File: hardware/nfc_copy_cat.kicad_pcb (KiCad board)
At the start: 2 copper layers, 40.4 x 43 mm, 33 parts, among them J1 USB_B_Micro, U1 AP2112K-3.3TRG1, U2 MCP73831-2-OT, U3 TC4424, U4 ATSAMD21E18A

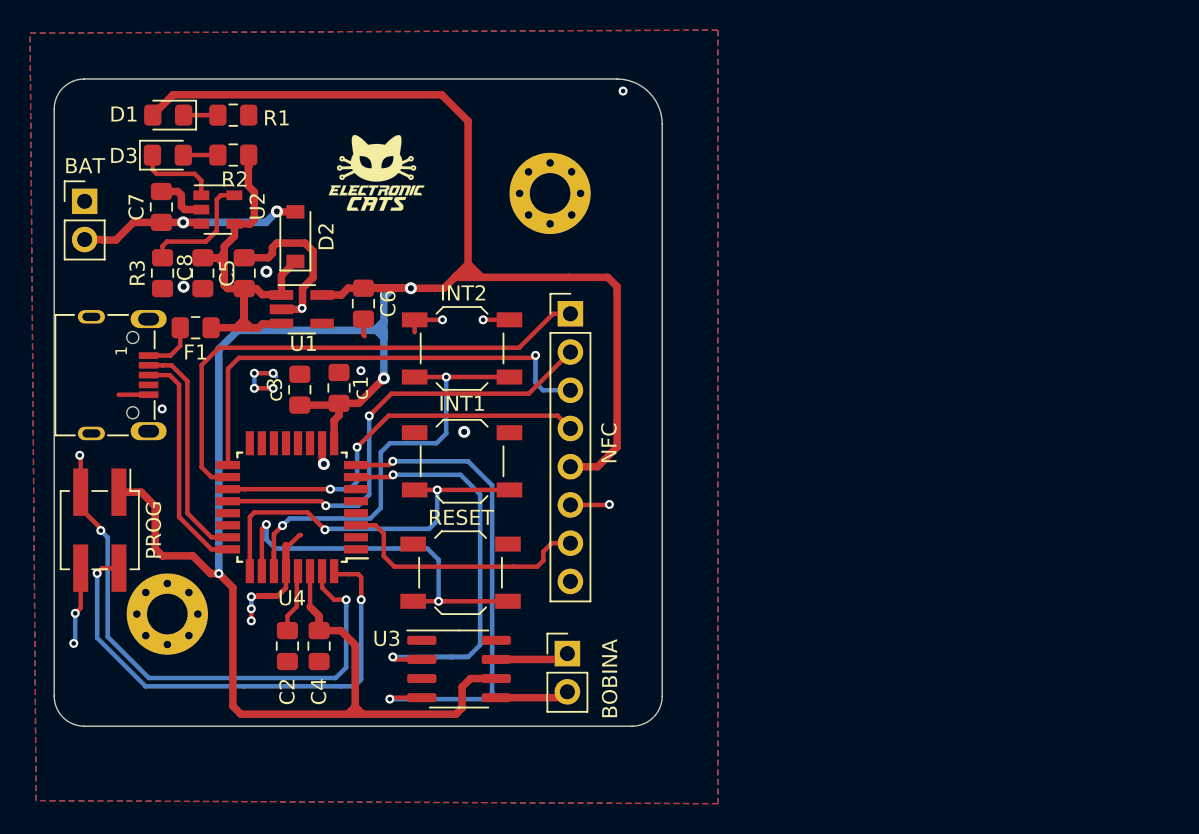
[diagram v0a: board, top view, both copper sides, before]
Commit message: añadimiento de led
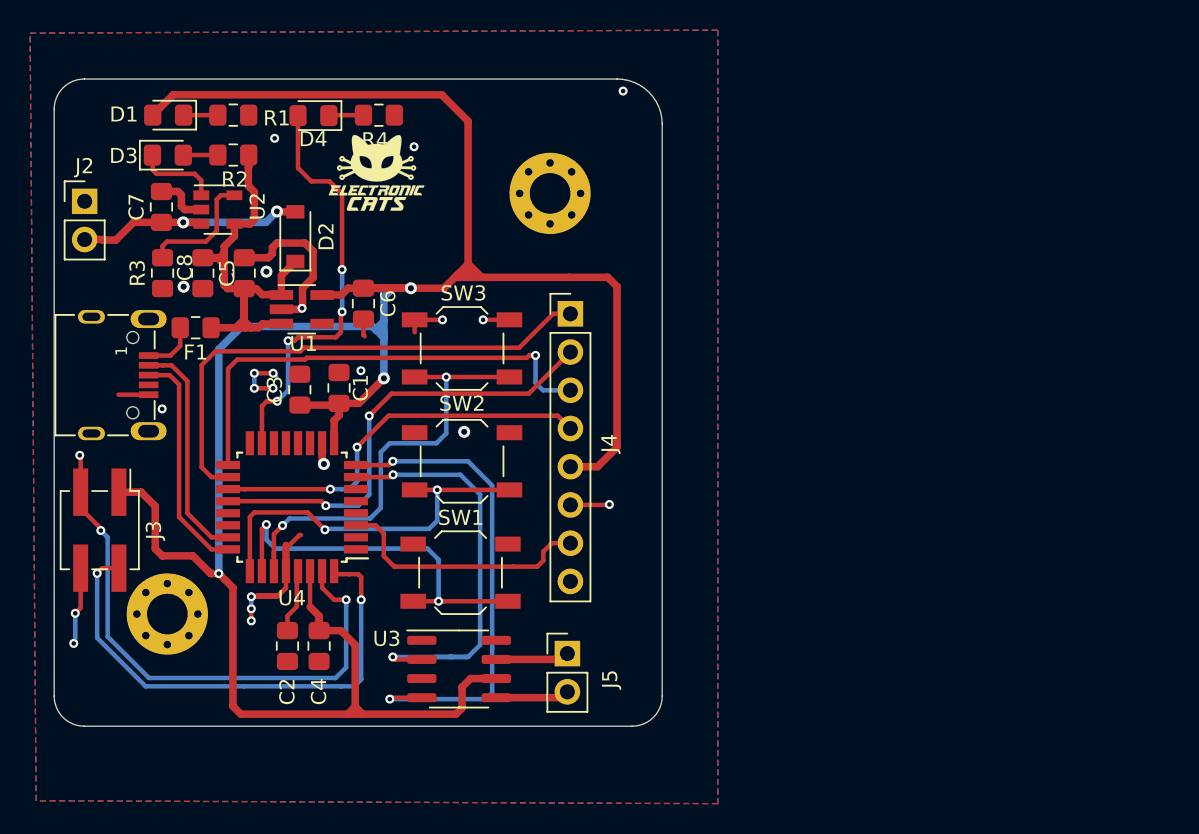
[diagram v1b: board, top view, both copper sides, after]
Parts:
- added D4: LED_Small, LED_SMD:LED_0805_2012Metric_Pad1.15x1.40mm_HandSolder, F.Cu at (144.9, 51.6)
- added R4: 330, Resistor_SMD:R_0805_2012Metric_Pad1.15x1.40mm_HandSolder, F.Cu at (149.3, 51.6)
- C4: value 0.1UF -> 0.1uf
- C6, C7, C8: value C -> 10uf
- R2: value R -> 1k
- R3: value R -> 2.2k
- renumbered c1 to C1, c3 to C3, BAT to J2, PROG to J3, NFC to J4, BOBINA to J5, RESET to SW1, INT1 to SW2, INT2 to SW3
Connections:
- U4 pad 15: Net-(U4-Pad15) -> /2(LED)
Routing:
- net /2(LED): track 0.00 -> 28.0 mm, vias 0 -> 4
- net Net-(D4-Pad1): track 0.00 -> 2.31 mm
- net GND: vias 20 -> 22

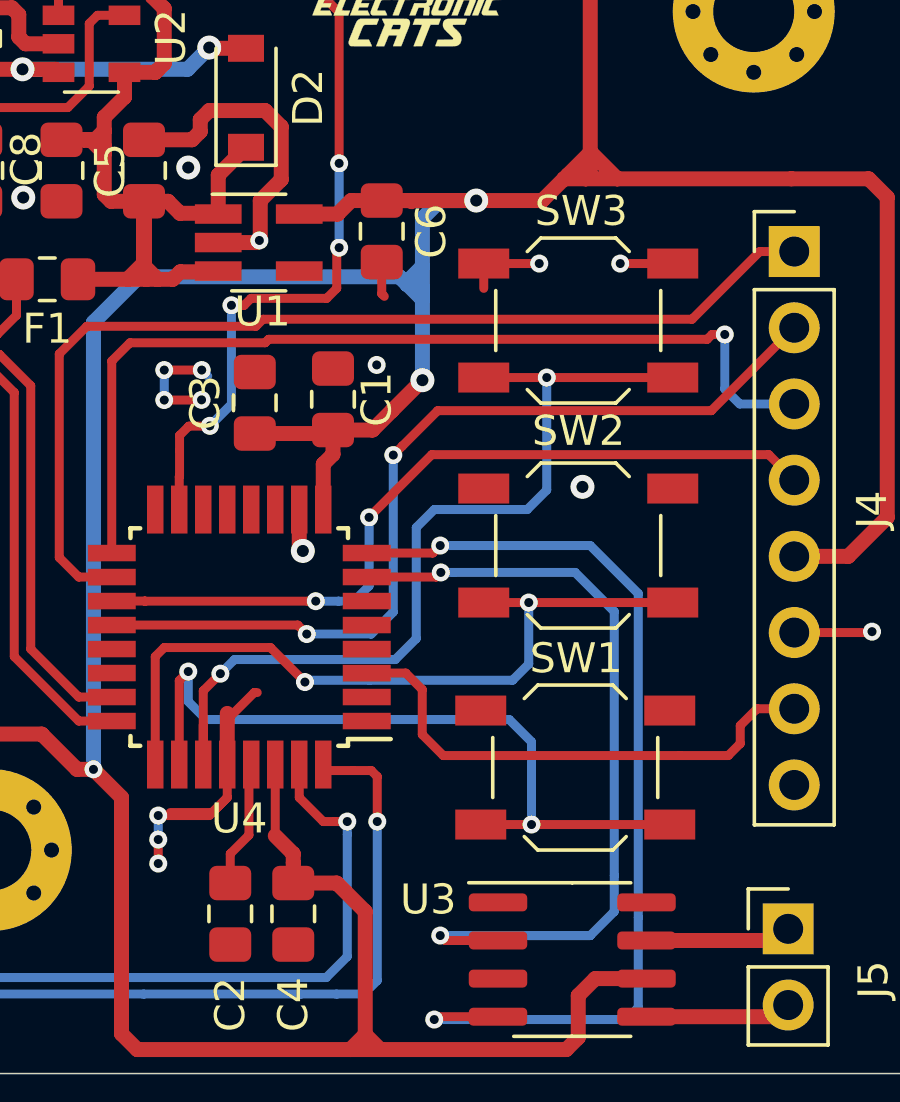
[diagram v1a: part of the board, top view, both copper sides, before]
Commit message: desplazamiento de botones haca atras
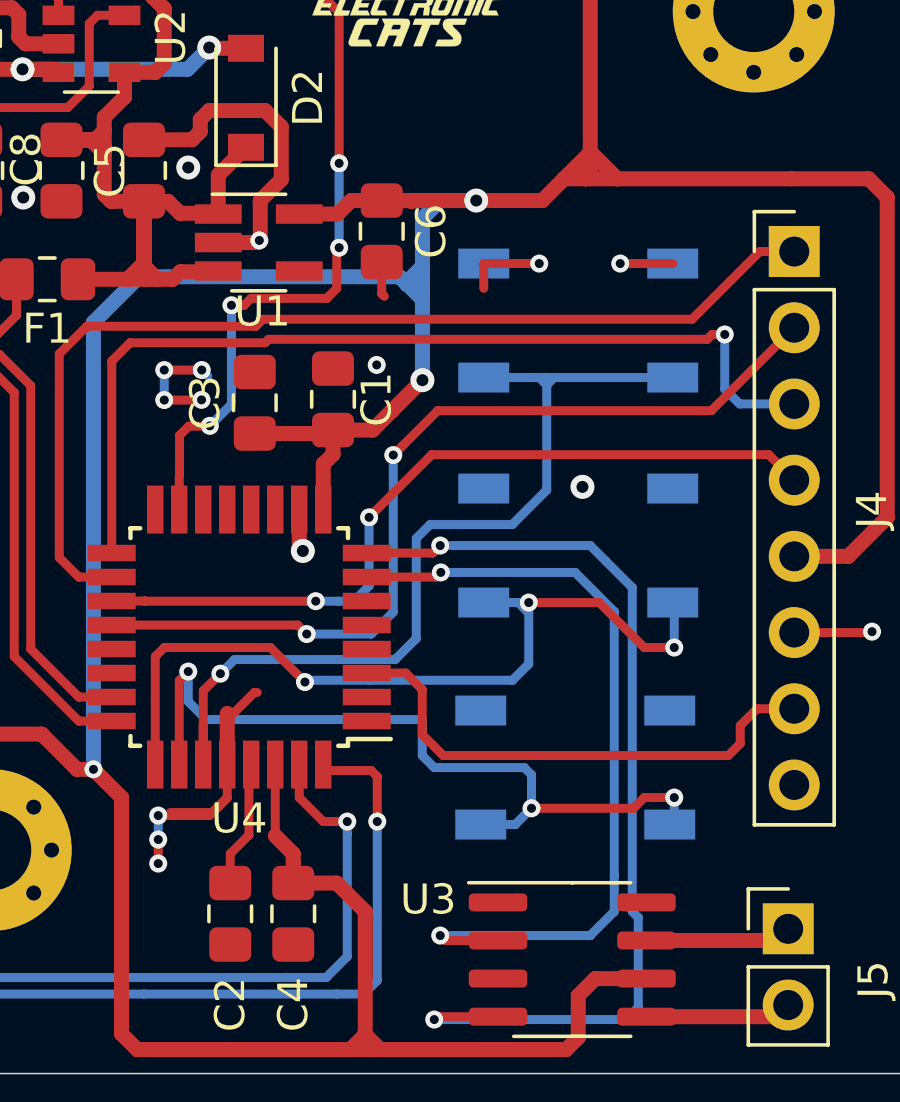
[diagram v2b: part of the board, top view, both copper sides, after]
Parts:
- SW1, SW2, SW3: moved to B.Cu
- turned SW1 to 0 degrees
- turned SW2 to 0 degrees
- turned SW3 to 0 degrees
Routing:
- net /SW1: track 25.2 -> 29.1 mm, vias 2 -> 3
- net /RESET: track 25.3 -> 26.9 mm, vias 2 -> 3
- net /SW2: track 30.2 -> 31.2 mm, vias 2 -> 1

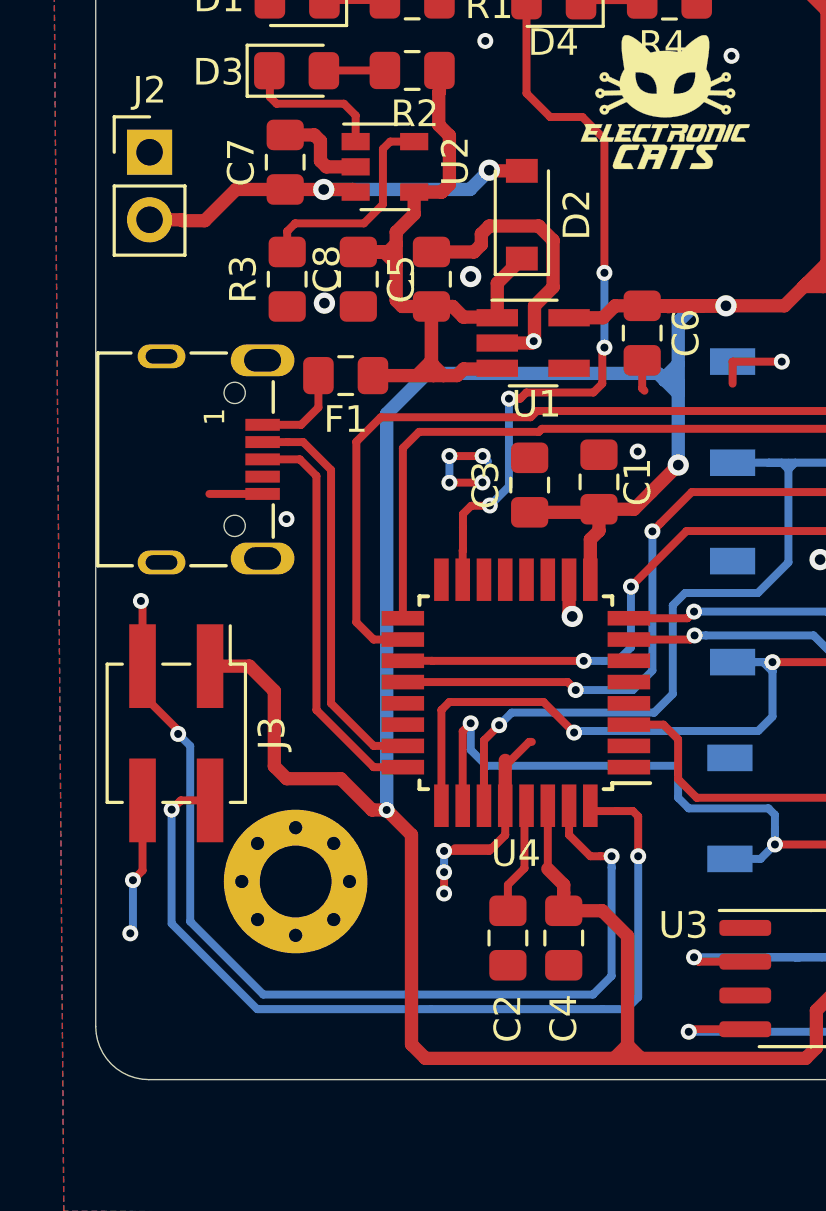
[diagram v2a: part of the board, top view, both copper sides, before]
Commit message: Update traces, USB port and version 1.3v
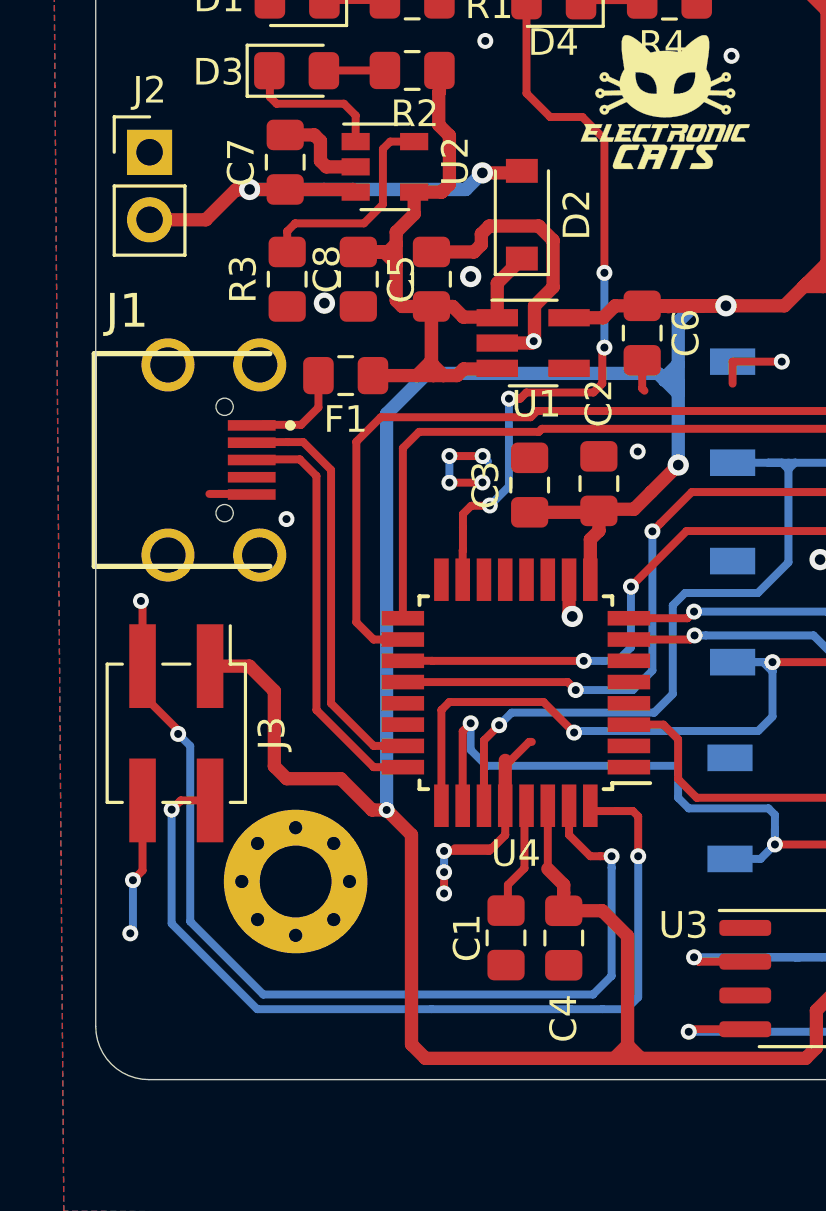
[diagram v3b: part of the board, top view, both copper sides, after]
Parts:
- D1: value LED_Small -> POWER
- D2: value D_Schottky -> MBR120
- D4: value LED_Small -> LED
- J1: footprint Connectors_EC:629105150521 -> Connectors:U254051N4BH806
- J2: value Screw_Terminal_01x02 -> Battery
- J4: value Conn_01x08 -> NFC Module V3
- SW1: value SW_DPST_x2 -> RST
- SW2: value SW_DPST_x2 -> Magspoof
- SW3: value SW_DPST_x2 -> NFC
- moved C1 17.5 mm to (143.1, 86.9), turned to 270 degrees
- moved C2 17.4 mm to (146.6, 69.8), turned to 90 degrees
- moved J1 1.54 mm to (131.4, 68.9)
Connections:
- net /2(LED) renamed /LED1
- net /BAT renamed +BATT
- net Net-(U4-Pad13) renamed /LED3
- net Net-(U4-Pad14) renamed /LED2
- C1 pad 1: +3V3 -> Net-(C1-Pad1)
- C2 pad 1: Net-(C2-Pad1) -> +3V3
- U4 pad 29: Net-(C2-Pad1) -> Net-(C1-Pad1)
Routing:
- net Net-(C2-Pad1): track 4.20 -> 0.00 mm
- net Net-(C1-Pad1): track 0.00 -> 4.20 mm
- net +BATT: track 16.1 -> 18.8 mm
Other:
- board text added: "NFC COPY CAT v1.2"
- board text removed: "NFC COPY CAT v0.1"

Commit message: nfc board v3
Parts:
- added D5: LED, LED_SMD:LED_0805_2012Metric_Pad1.15x1.40mm_HandSolder, F.Cu at (144.8, 54.2)
- added D6: LED, LED_SMD:LED_0805_2012Metric_Pad1.15x1.40mm_HandSolder, F.Cu at (155.7, 51.6)
- added J6: Adafruit NFC 1.0, Connector_PinHeader_2.54mm:PinHeader_1x09_P2.54mm_Vertical, F.Cu at (165.8, 82.6)
- added R5: 330, Resistor_SMD:R_0805_2012Metric_Pad1.15x1.40mm_HandSolder, F.Cu at (149.1, 54.2)
- added R6: 330, Resistor_SMD:R_0805_2012Metric_Pad1.15x1.40mm_HandSolder, F.Cu at (155.7, 54.0)
- J3: value Conn_02x02_Counter_Clockwise -> SWD; footprint Connector_PinHeader_2.54mm:PinHeader_2x02_P2.54mm_Vertical_SMD -> Connector_PinHeader_2.54mm:PinHeader_1x04_P2.54mm_Vertical; moved to B.Cu
- SW1, SW2, SW3: moved to F.Cu
- moved G*** 38.0 mm to (131.0, 88.8)
- moved J4 17.8 mm to (162.1, 82.6), turned to 180 degrees
- moved C5 6.87 mm to (138.5, 68.7), turned to 180 degrees
- moved J3 3.20 mm to (129.5, 76.2), turned to 180 degrees
- moved SW2 1.09 mm to (153.7, 74.7), turned to 180 degrees
- moved SW3 1.09 mm to (153.7, 67.2), turned to 180 degrees
- moved SW1 1.09 mm to (153.6, 82.1), turned to 180 degrees
- moved C6 1.02 mm to (147.2, 64.2)
- moved U1 1.02 mm to (143.1, 64.6)
- moved U4 0.97 mm to (142.5, 77.5)
- moved C3 0.90 mm to (143.1, 69.9)
- moved C2 0.90 mm to (145.7, 69.9)
- moved D1 0.78 mm to (134.5, 51.6)
- moved D3 0.71 mm to (134.6, 54.1)
- moved U2 0.07 mm to (138.6, 57.8)
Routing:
- net /12(MISO): track 30.2 -> 73.3 mm, vias 2 -> 3
- net GND: track 47.1 -> 87.0 mm, vias 22 -> 29
- net /LED3: track 0.00 -> 36.9 mm, vias 0 -> 2
- net /13(SCK): track 34.7 -> 65.3 mm, vias 0 -> 1
- net /LED2: track 0.00 -> 29.5 mm, vias 0 -> 2
- net /IRQ: track 17.3 -> 38.5 mm, vias 0 -> 1
- net /SWCLK: track 37.6 -> 25.0 mm, vias 3 -> 1
- net /10(SS): track 26.5 -> 36.6 mm
- net /11(MOSI): track 31.5 -> 40.4 mm, vias 1 -> 2
- net /IN_A: track 29.4 -> 20.6 mm, vias 2 -> 0
- net /IN_B: track 32.7 -> 24.7 mm, vias 2 -> 0
- net /SWDIO: track 33.7 -> 26.0 mm, vias 2 -> 1
- net +3V3: track 171.0 -> 163.5 mm, vias 3 -> 4
- net +BATT: track 18.8 -> 23.9 mm
- net VCC: track 31.4 -> 35.2 mm
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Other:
- net class sourse: clearance 0.4 -> 0.2
- board text added: "NFC COPY CAT v1.3"
- board text removed: "NFC COPY CAT v1.2"

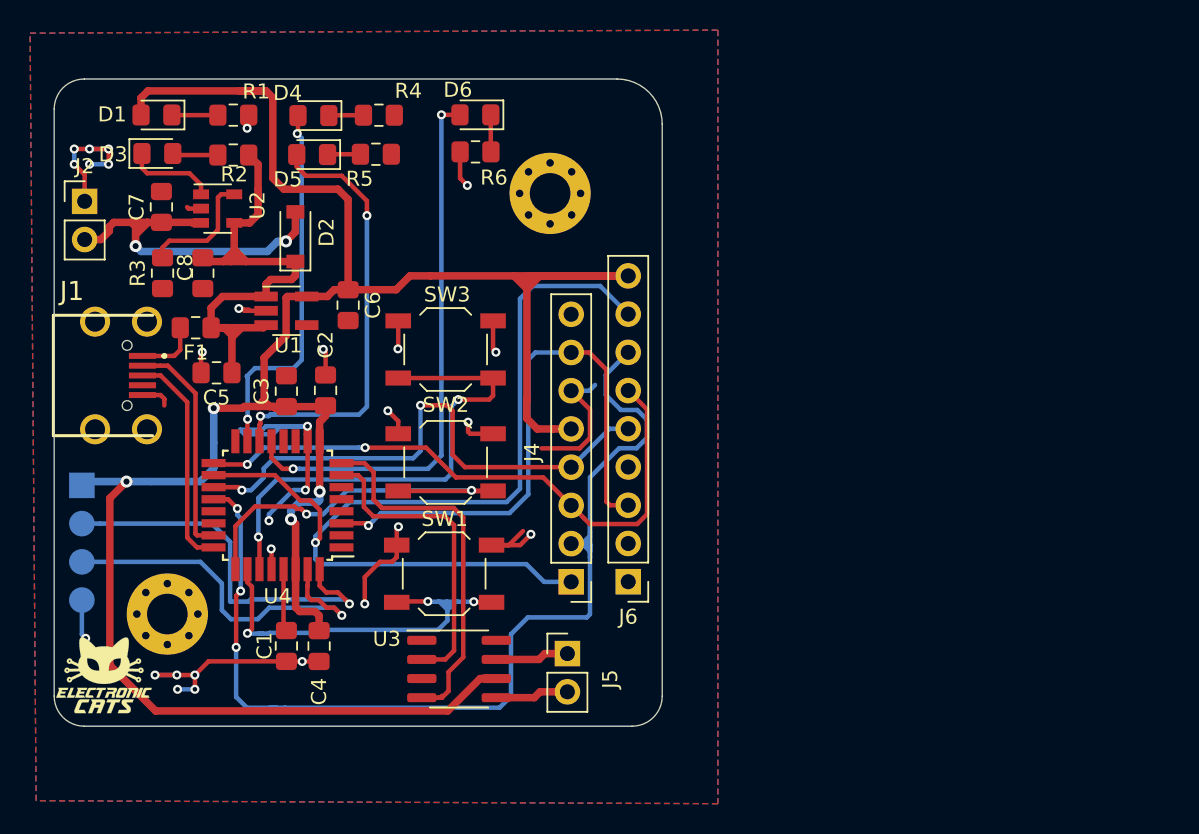
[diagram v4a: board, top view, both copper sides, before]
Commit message: add labels pinout
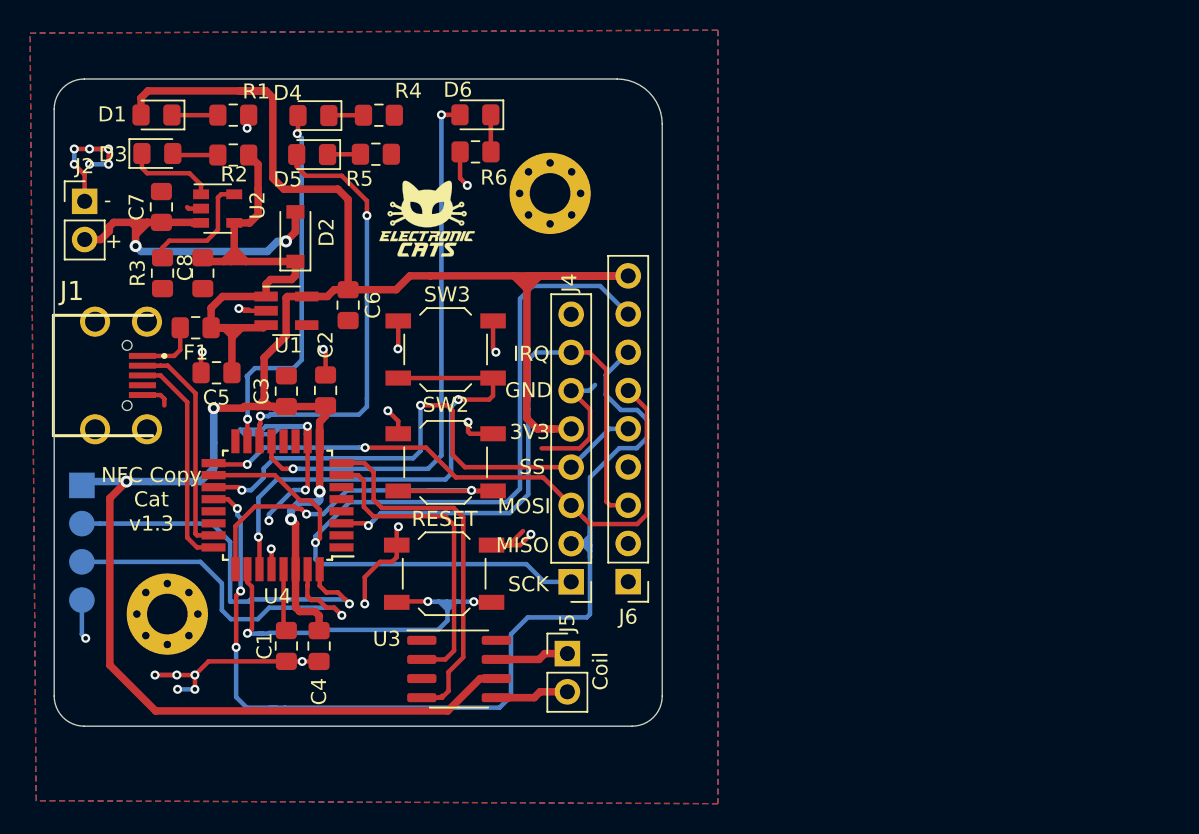
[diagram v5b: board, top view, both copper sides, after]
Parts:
- removed the G*** at (146.7, 62.6)
- moved G*** 37.2 mm to (152.5, 58.5)
- renumbered SW1 to RESET
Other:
- board text added: "+"
- board text added: "-"
- board text added: "3V3"
- board text added: "Coil"
- board text added: "GND"
- board text added: "IRQ"
- board text added: "MI"
- board text added: "MISO"
- board text added: "MO"
- board text added: "MOSI"
- board text added: "NFC Copy Cat v1.3"
- board text added: "SCK"
- board text added: "SS"
- board text added: "battery"
